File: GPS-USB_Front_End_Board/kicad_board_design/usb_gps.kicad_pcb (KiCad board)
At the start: 4 copper layers, 99.1 x 53.3 mm, 91 parts, among them J1 Micro-USB Connector, J3 Edge Launch SMA, P1 CONN_02X12, U1 93LCxxB, U2 FT2232HL-REEL, U3 L4931 LDO, U4 MAX8510, U5 MAX8510, U6 MAX2769CETI+, U7 SAWTEK-855969, U8 LT1719S6 -- Not Populated, X1 13.368MHz TCXO, Y1 12MHz Crystal

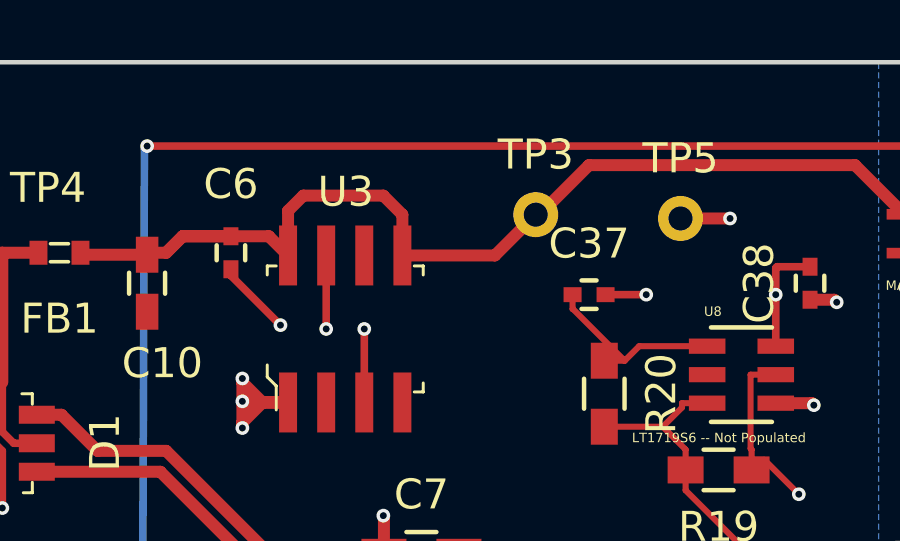
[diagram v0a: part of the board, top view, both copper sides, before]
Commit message: Fix 3.3V LDO inhibit polarity.
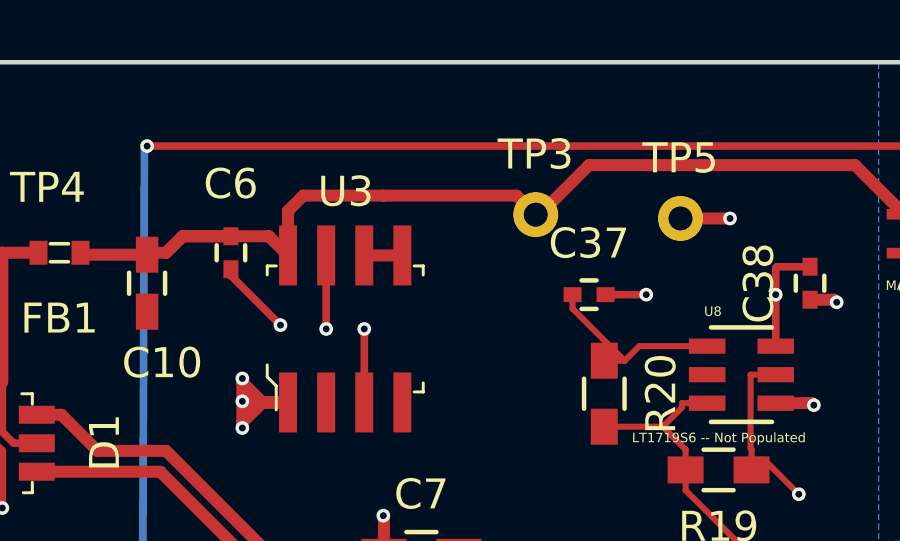
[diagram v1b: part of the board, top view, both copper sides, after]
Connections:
- U3 pad 5: /MAX_2769/+5V -> GND
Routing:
- net /MAX_2769/+5V: track 114.0 -> 112.1 mm
- net GND: track 102.1 -> 103.4 mm
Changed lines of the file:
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@@
     (links 222)
     (no_connects 0)
-    (area 79.665 60.884999 184.249448 115.135)
+    (area 82.474999 60.884999 181.685001 114.375001)
     (thickness 1.6)
     (drawings 5)
-    (tracks 976)
+    (tracks 975)
     (zones 0)
     (modules 91)
@@
   )
   (setup
-    (last_trace_width 0.2032)
+    (last_trace_width 0.4)
     (user_trace_width 0.254)
     (user_trace_width 0.399999)
@@
       (net 84 "Net-(U3-Pad4)"))
     (pad 5 smd rect (at 1.905 -2.45) (size 0.6 2) (layers F.Cu F.Paste F.Mask)
-      (net 5 /MAX_2769/+5V))
+      (net 1 GND))
     (pad 6 smd rect (at 0.635 -2.45) (size 0.6 2) (layers F.Cu F.Paste F.Mask)
       (net 1 GND))
@@
   (via (at 146.95 89.35) (size 0.4572) (drill 0.254) (layers F.Cu B.Cu) (net 0))
   (segment (start 146.9 89.3) (end 146.95 89.35) (width 0.2032) (layer F.Cu) (net 0))
+  (segment (start 111.125 67.4) (end 109.855 67.4) (width 0.4) (layer F.Cu) (net 1) (status C00000))
   (segment (start 158.03 111.76) (end 158.03 110.8876) (width 0.399999) (layer F.Cu) (net 1))
   (segment (start 157.6324 110.49) (end 150.99 110.49) (width 0.399999) (layer F.Cu) (net 1))
@@
   (segment (start 113.24 85.6479) (end 113.24 84.42) (width 0.2032) (layer F.Cu) (net 4))
   (segment (start 113.3921 85.8) (end 113.24 85.6479) (width 0.2032) (layer F.Cu) (net 4))
+  (segment (start 110.49 65.405) (end 114.935 65.405) (width 0.4) (layer F.Cu) (net 5))
+  (segment (start 107.315 67.4) (end 107.315 65.913) (width 0.4) (layer F.Cu) (net 5))
+  (segment (start 107.315 65.913) (end 107.823 65.405) (width 0.4) (layer F.Cu) (net 5))
+  (segment (start 107.823 65.405) (end 110.49 65.405) (width 0.4) (layer F.Cu) (net 5))
+  (segment (start 114.935 65.405) (end 115.57 66.04) (width 0.4) (layer F.Cu) (net 5) (status 800000))
   (segment (start 102.616 67.376) (end 100.461 67.376) (width 0.399999) (layer F.Cu) (net 5))
   (segment (start 100.461 67.376) (end 100.395 67.31) (width 0.399999) (layer F.Cu) (net 5))
@@
   (via (at 129.794 68.199) (size 0.4572) (layers F.Cu B.Cu) (net 5))
   (via (at 129.794 69.342) (size 0.4572) (layers F.Cu B.Cu) (net 5))
-  (segment (start 111.125 66.04) (end 111.125 67.4) (width 0.4) (layer F.Cu) (net 5))
-  (segment (start 110.49 65.405) (end 111.125 66.04) (width 0.4) (layer F.Cu) (net 5))
-  (segment (start 107.823 65.405) (end 110.49 65.405) (width 0.4) (layer F.Cu) (net 5))
-  (segment (start 107.315 65.913) (end 107.823 65.405) (width 0.4) (layer F.Cu) (net 5))
-  (segment (start 107.315 67.4) (end 107.315 65.913) (width 0.4) (layer F.Cu) (net 5))
   (segment (start 129.794 69.342) (end 129.794 80.645) (width 0.254) (layer B.Cu) (net 5))
   (segment (start 129.54 71.501) (end 129.54 70.932) (width 0.254) (layer F.Cu) (net 5) (status 20))
@@
   (segment (start 115.697 66.04) (end 117.348 64.389) (width 0.4) (layer F.Cu) (net 5))
   (segment (start 115.57 66.04) (end 115.697 66.04) (width 0.4) (layer F.Cu) (net 5))
-  (segment (start 114.21 67.4) (end 115.57 66.04) (width 0.4) (layer F.Cu) (net 5))
-  (segment (start 111.125 67.4) (end 114.21 67.4) (width 0.4) (layer F.Cu) (net 5))
   (segment (start 103.251 67.31) (end 103.801 66.76) (width 0.4) (layer F.Cu) (net 5))
   (segment (start 103.251 67.31) (end 103.801 66.76) (width 0.4) (layer F.Cu) (net 5))

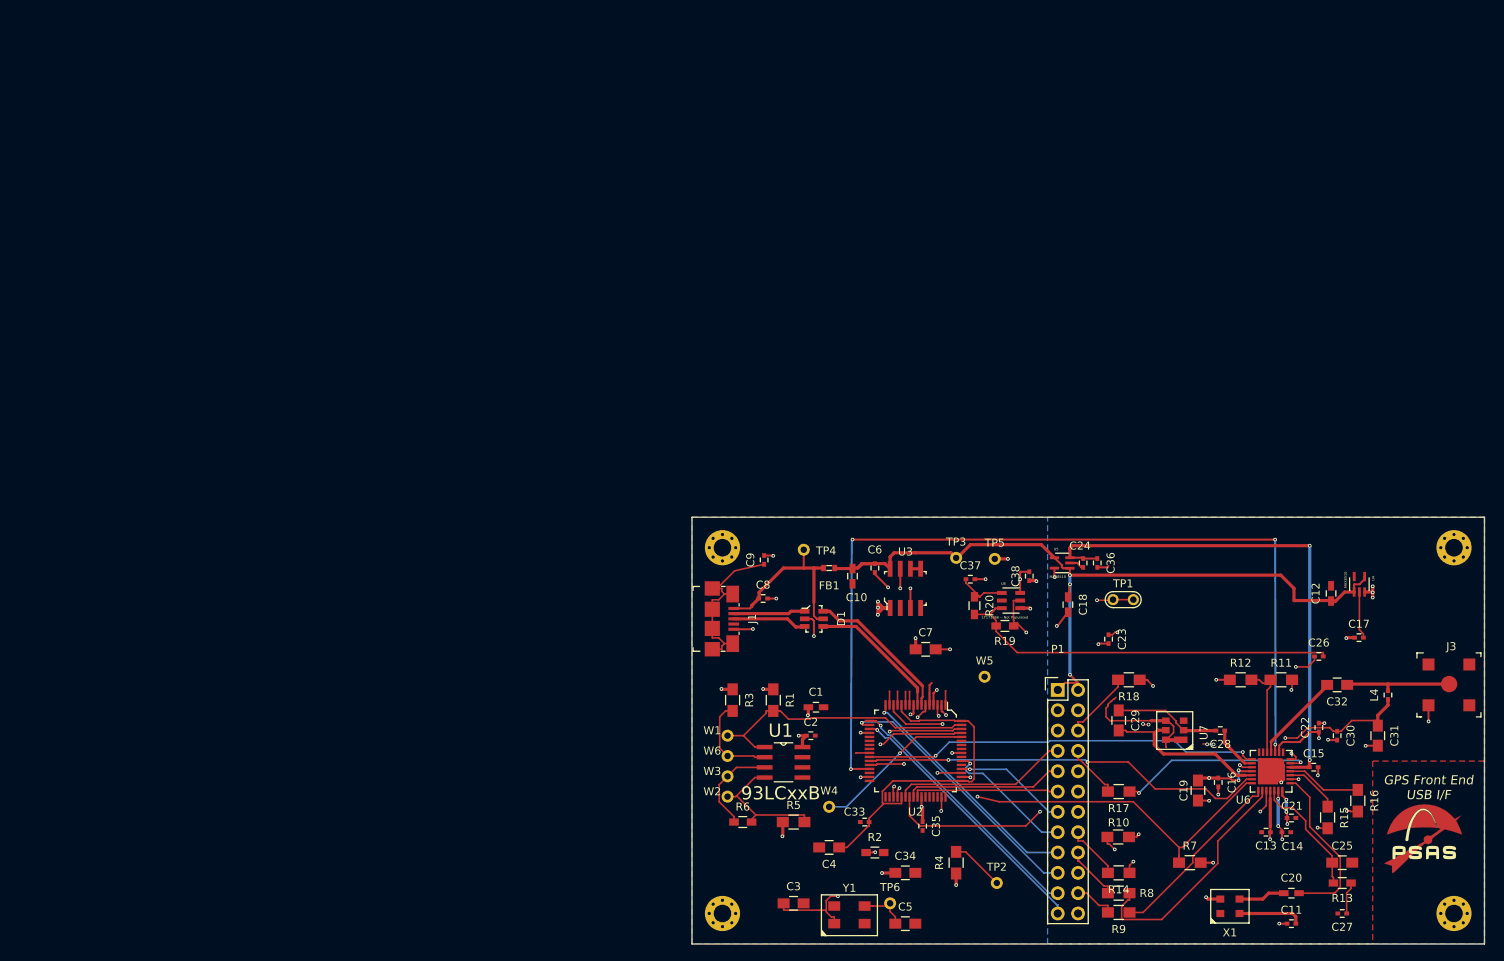
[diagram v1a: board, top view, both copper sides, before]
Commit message: Fix footprint for MAX 8510 (two places).
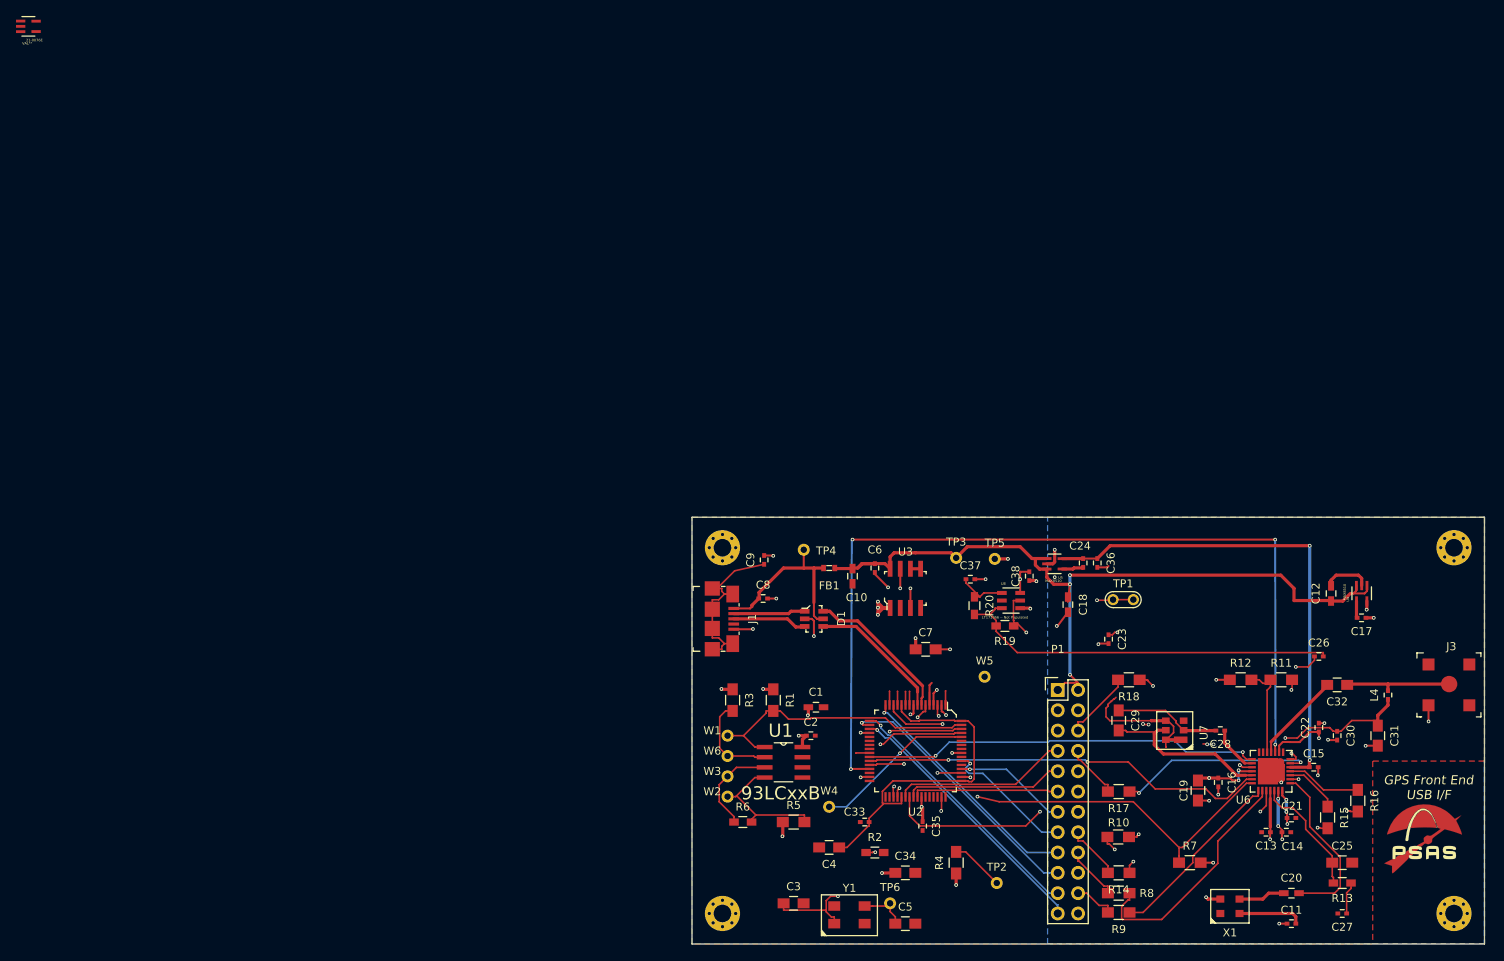
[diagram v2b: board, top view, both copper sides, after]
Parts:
- added 21-0076E: VAL**, 21-0076E, F.Cu at (0.00, 0.00)
- U4, U5: footprint rf:21-0076E -> rf:21-0076E_FLIP
- moved C17 2.50 mm to (166.2, 73.5), turned to 180 degrees
- moved U4 1.53 mm to (165.9, 70.9)
- moved U5 0.75 mm to (128.3, 67.2)
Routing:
- net GND: track 103.4 -> 110.7 mm
- net Net-(C17-Pad2): track 5.91 -> 2.13 mm
- net /MAX_2769/VCCD: track 65.0 -> 61.9 mm
- net /MAX_2769/+5V: track 112.1 -> 114.0 mm
- net /MAX_2769/VCCA: track 43.8 -> 41.9 mm, vias 20 -> 18
- net (no net): track 3.05 -> 4.88 mm, vias 4 -> 5
- net Net-(C24-Pad2): track 1.89 -> 2.91 mm

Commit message: Change out micro-usb connector to one with thru holes.
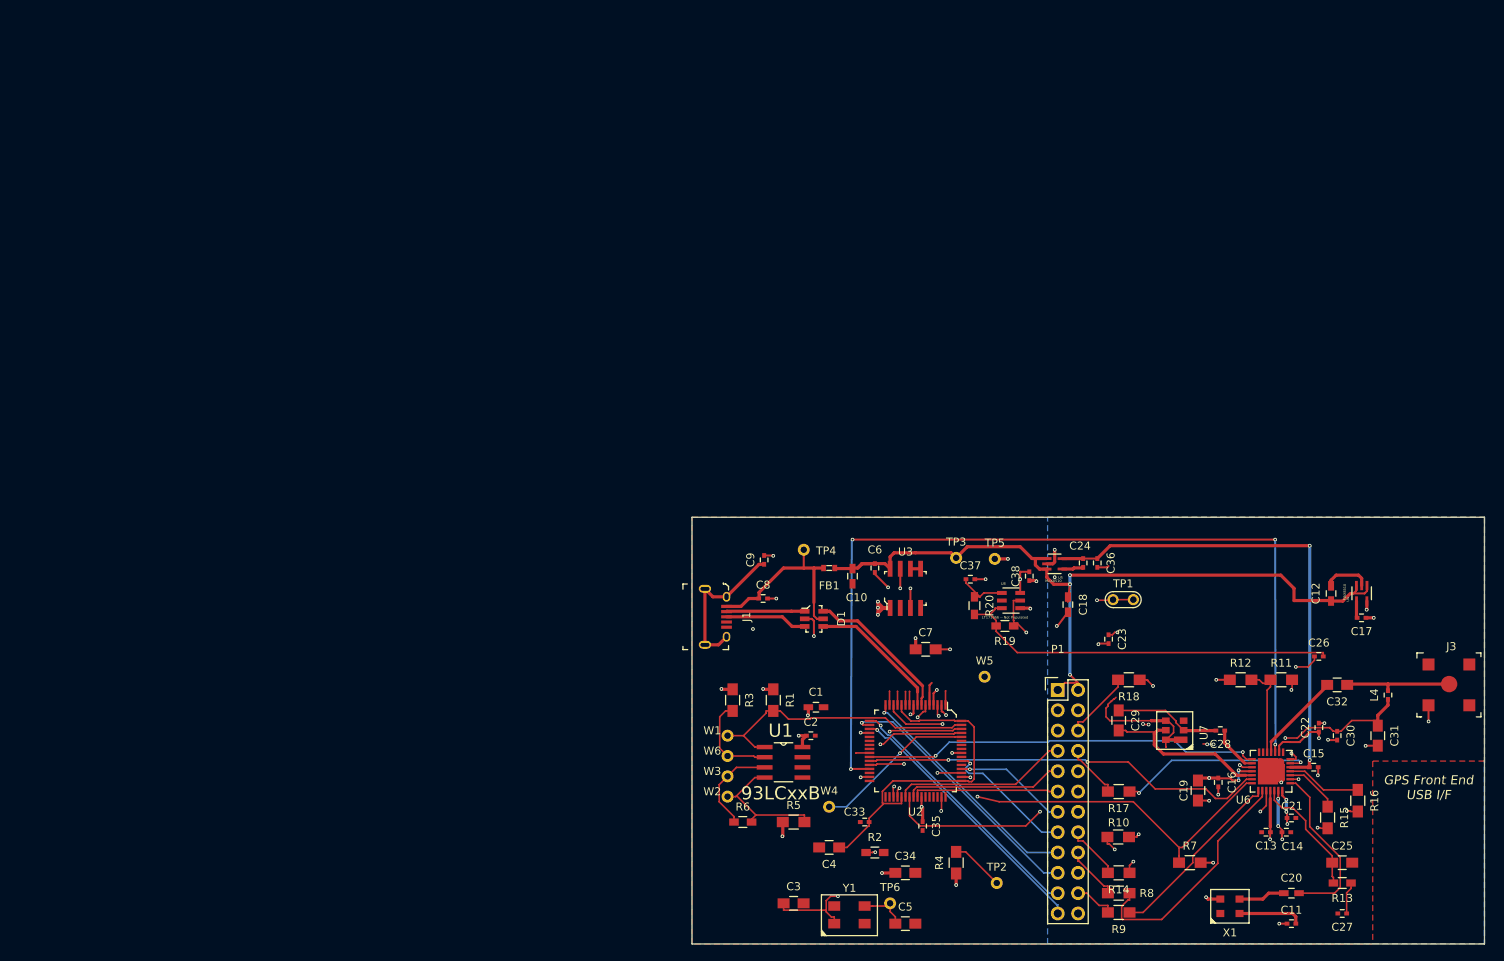
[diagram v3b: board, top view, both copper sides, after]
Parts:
- removed 21-0076E: VAL**, 21-0076E
- removed G***: LOGO, logo:logo_combined_components
- removed REF** (x4): MountingHole_2.2mm_M2_Pad_Via, Mounting_Holes:MountingHole_2.2mm_M2_Pad_Via
- J1: footprint digikey-footprints:USB_Micro_B_Female_10118192 -> digikey-footprints:USB_Micro_B_Female_10118194-0001LF
- moved J1 1.80 mm to (86.9, 73.4)
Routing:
- net GND: track 110.7 -> 108.3 mm, vias 26 -> 25
- net Net-(C9-Pad1): track 21.4 -> 19.6 mm
- net Net-(D1-Pad3): track 9.32 -> 10.4 mm
- net Net-(D1-Pad1): track 9.00 -> 9.86 mm
- net /USB_FT2232/VBUS: track 23.4 -> 24.1 mm
- net (no net): track 4.88 -> 4.93 mm, vias 5 -> 6
